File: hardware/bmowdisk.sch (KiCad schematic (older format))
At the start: 41 parts, among them CON1 IDC20, J1 MA06-1NORMAL, J2 MA04-1S, J3 LCD1, J4 M02PTH, U1 LCMXO2-1200HC-TQFP100, U2 SPI-FLASH, U3 MIC5219XX, U4 74X245, U5 74X245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

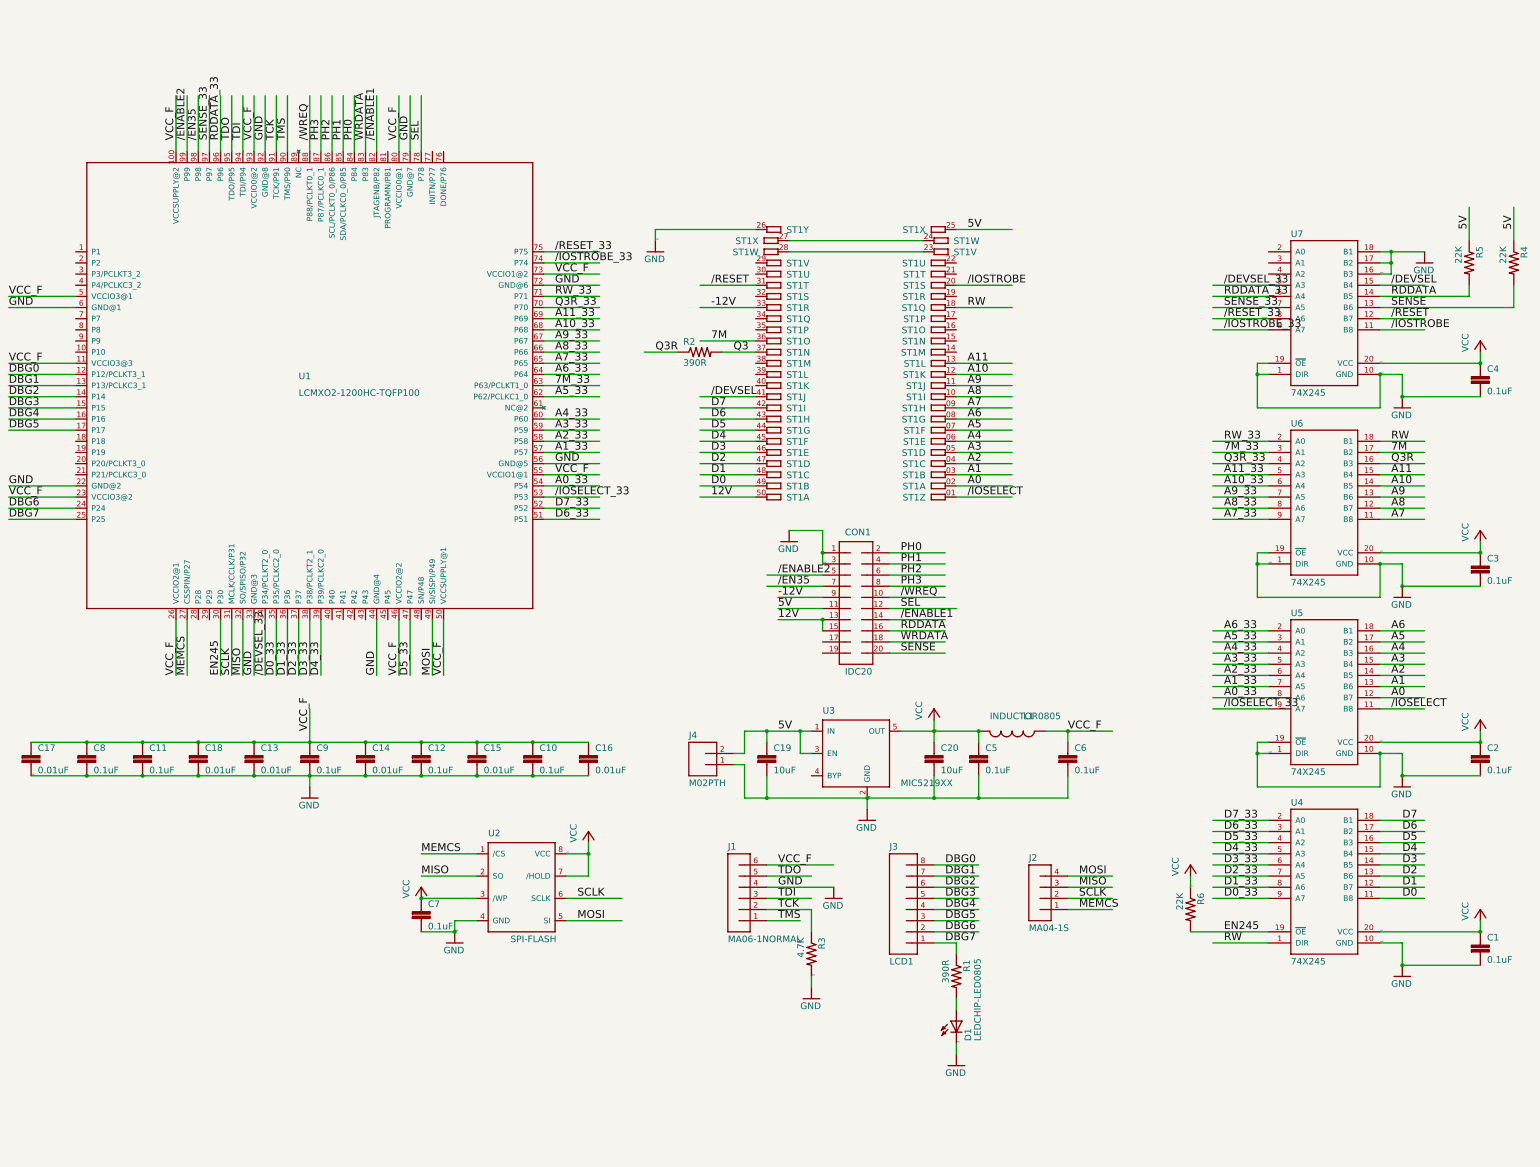
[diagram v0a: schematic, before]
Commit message: Tidy up schematics, remove machxo2 FPGA and related components
Initial prototype version with headers for connecting olimex ice40-hx8k
fpga dev board for replacing the fpga

Signed-off-by: Rangel Ivanov <rangelivanov88@gmail.com>
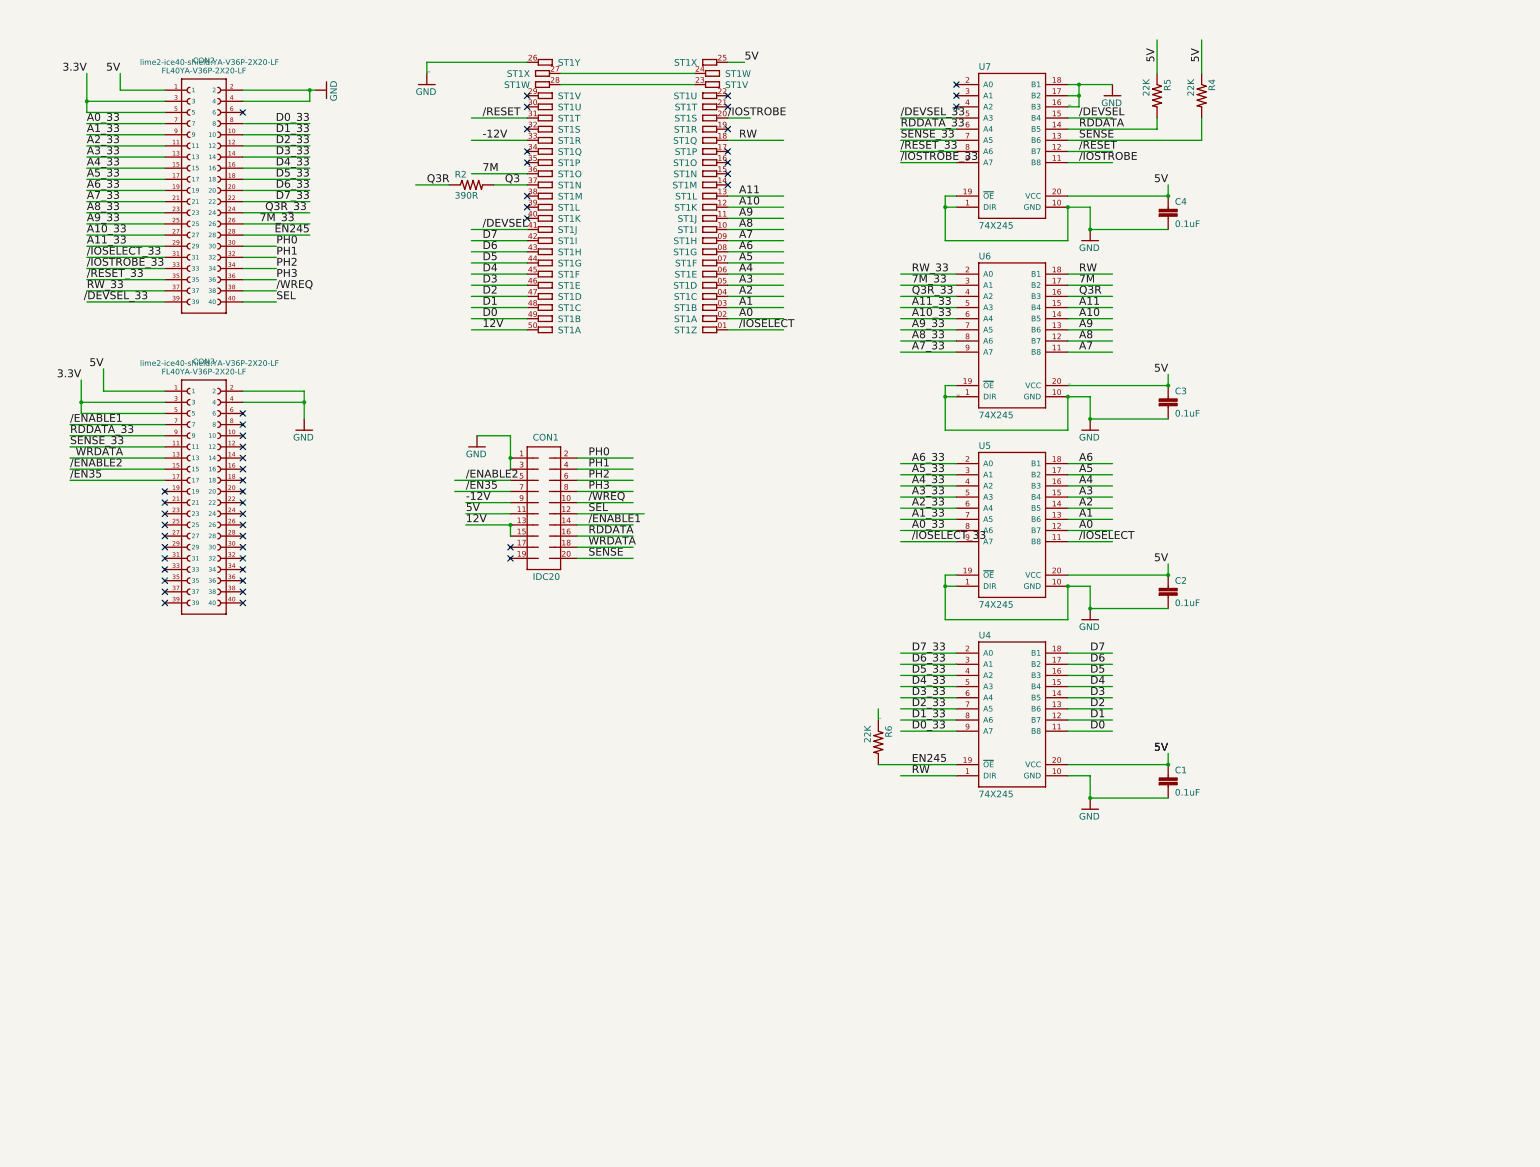
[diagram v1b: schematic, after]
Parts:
- removed C10, C11, C12, C5, C6, C7, C8, C9: 0.1uF, bmowdisk:0805, symbol bmowdisk-eagle-import:CAP0805
- removed C13, C14, C15, C16, C17, C18: 0.01uF, bmowdisk:0805, symbol bmowdisk-eagle-import:CAP0805
- removed C19, C20: 10uF, bmowdisk:0805, symbol bmowdisk-eagle-import:CAP0805
- removed D1: LEDCHIP-LED0805, bmowdisk:CHIP-LED0805, symbol bmowdisk-eagle-import:LEDCHIP-LED0805
- removed J1: MA06-1NORMAL, bmowdisk:MA06-1, symbol bmowdisk-eagle-import:MA06-1NORMAL
- removed J2: MA04-1S, bmowdisk:MA04-1, symbol bmowdisk-eagle-import:MA04-1S
- removed J3: LCD1, bmowdisk:1X08, symbol bmowdisk-eagle-import:M081X08
- removed J4: M02PTH, bmowdisk:1X02, symbol bmowdisk-eagle-import:M02PTH
- removed L1: INDUCTOR0805, bmowdisk:0805, symbol bmowdisk-eagle-import:INDUCTOR0805
- removed R1: 390R, bmowdisk:0805, symbol bmowdisk-eagle-import:RESISTOR0805-RES
- removed R3: 4.7K, bmowdisk:0805, symbol bmowdisk-eagle-import:RESISTOR0805-RES
- removed U1: LCMXO2-1200HC-TQFP100, bmowdisk:TQFP100, symbol bmowdisk-eagle-import:LCMXO2-1200HC-TQFP100
- removed U2: SPI-FLASH, bmowdisk:SOIC08, symbol bmowdisk-eagle-import:SPI-FLASH
- removed U3: MIC5219XX, bmowdisk:SOT23-5, symbol bmowdisk-eagle-import:MIC5219XX
- added CON2, CON3: FL40YA-V36P-2X20-LF, lime2-ice40-shield:YA-V36P-2X20-LF, symbol ice40-shield-lib:FL40YA-V36P-2X20-LF
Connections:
- net labels added: 3.3V
- net labels removed: DBG0, DBG1, DBG2, DBG3, DBG4, DBG5, DBG6, DBG7, MEMCS, MISO, MOSI, SCLK, TCK, TDI, TDO, TMS, VCC_F
- wire segments 323 -> 223
- no-connect marks 0 -> 50
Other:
- moved on the sheet: C1, C2, C3, C4, CON1, R2, R4, R5, R6, ST1A, ST1B, ST1C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

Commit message: Replace 74X245 with SN74LVC8T245PW
Signed-off-by: Rangel Ivanov <rangelivanov88@gmail.com>
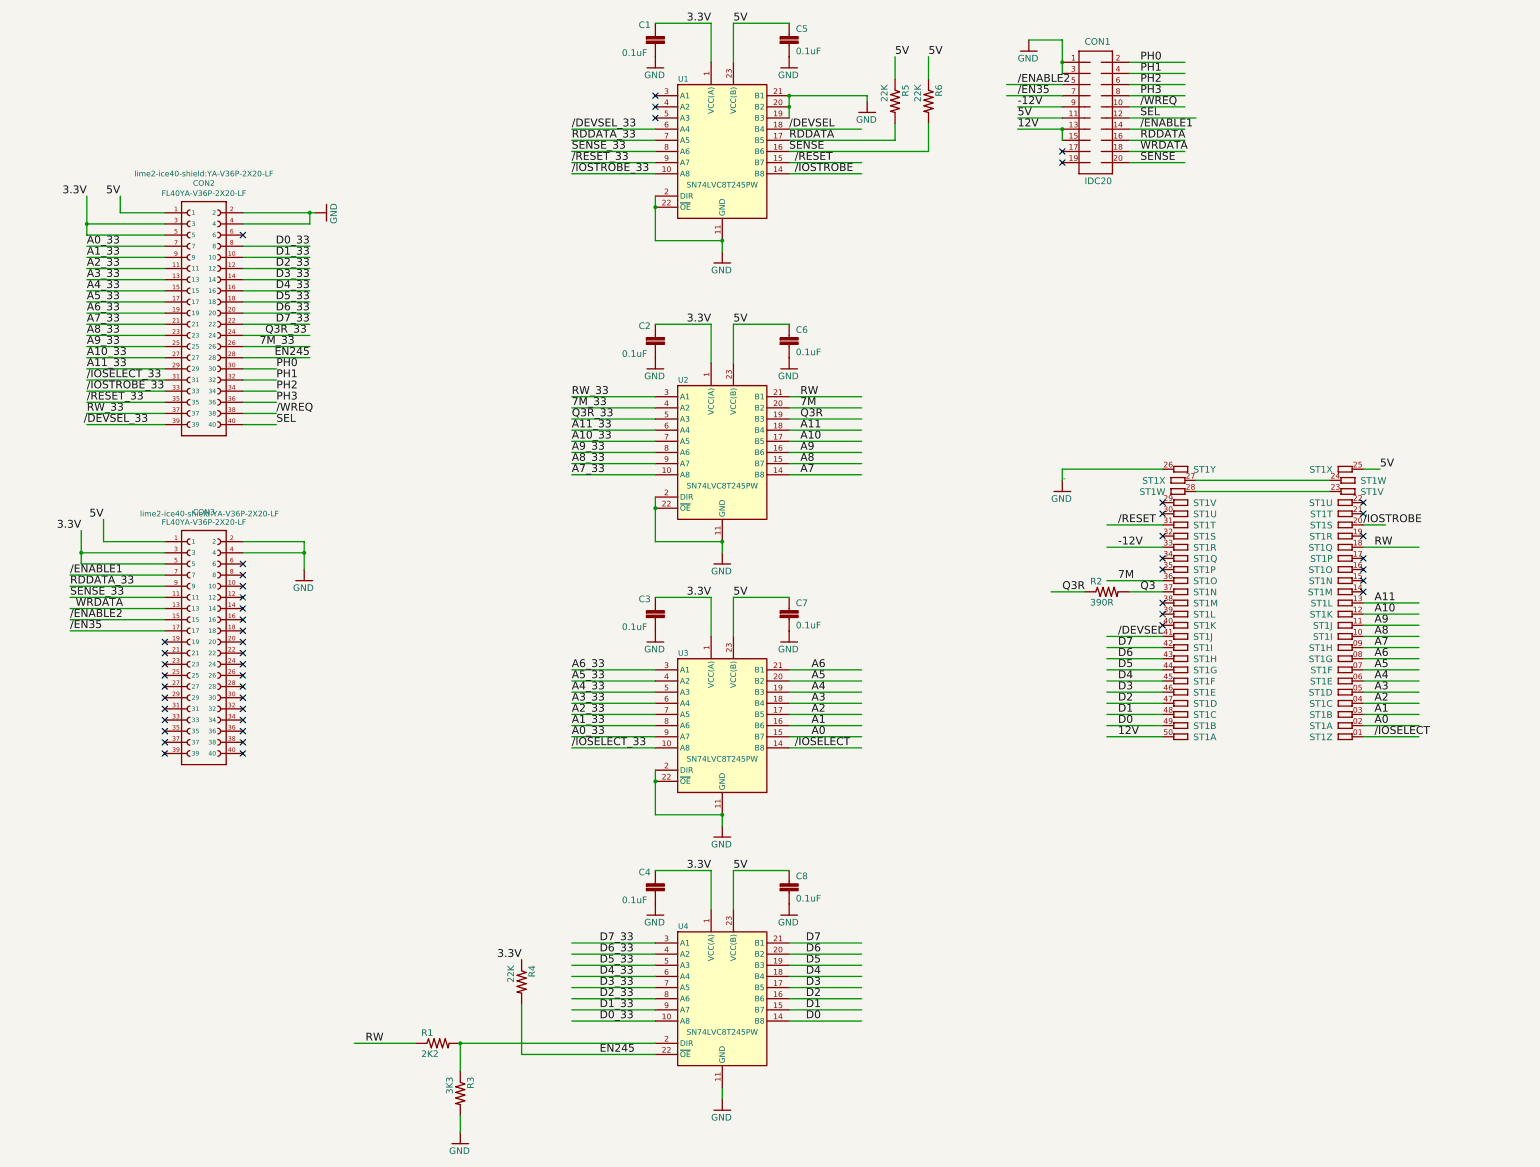
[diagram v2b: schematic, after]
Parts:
- removed U4, U5, U6, U7: 74X245, bmowdisk:SSOP20, symbol bmowdisk-eagle-import:74X245
- added C5, C6, C7, C8: 0.1uF, bmowdisk:0805, symbol bmowdisk-eagle-import:CAP0805
- added R1: 2K2, bmowdisk:0805, symbol bmowdisk-eagle-import:RESISTOR0805-RES
- added R3: 3K3, bmowdisk:0805, symbol bmowdisk-eagle-import:RESISTOR0805-RES
- added U1, U2, U3, U4: SN74LVC8T245PW, Package_SO:TSSOP-24_4.4x7.8mm_P0.65mm, symbol bmowdisk-eagle-import:SN74LVC8T245PW
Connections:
- net labels removed: VCC
- wire segments 223 -> 215
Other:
- moved on the sheet: CON1, CON2, CON3, R2, ST1A, ST1B, ST1C, ST1D, ST1E, ST1F, ST1G, ST1H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

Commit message: Lower text size of labels
Use ~ for active low labels/signals

Add TSSOP-24_4.4x7.8mm_P0.65mm footprint to project specific libs

Signed-off-by: Rangel Ivanov <rangelivanov88@gmail.com>
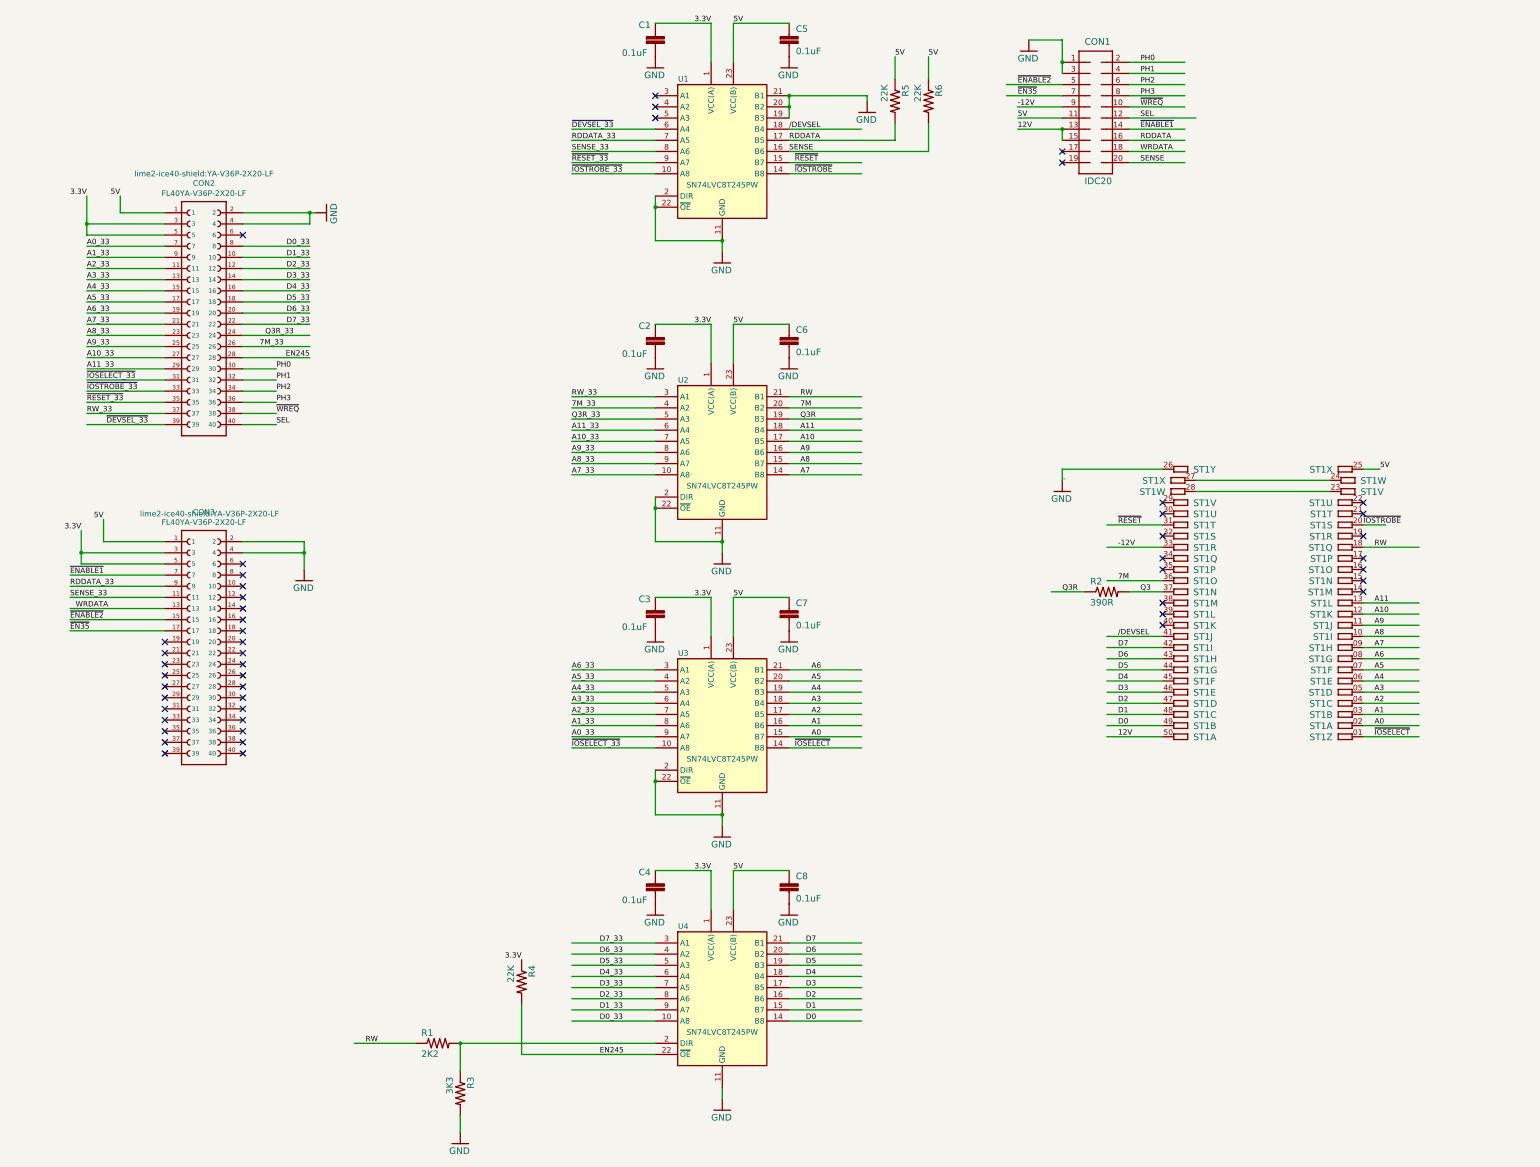
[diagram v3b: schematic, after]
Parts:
- U1, U2, U3, U4: footprint Package_SO:TSSOP-24_4.4x7.8mm_P0.65mm -> bmowdisk:TSSOP-24_4.4x7.8mm_P0.65mm
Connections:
- net labels added: ~DEVSEL_33, ~EN35, ~ENABLE1, ~ENABLE2, ~IOSELECT, ~IOSELECT_33, ~IOSTROBE, ~IOSTROBE_33, ~RESET, ~RESET_33, ~WREQ
- net labels removed: /DEVSEL_33, /EN35, /ENABLE1, /ENABLE2, /IOSELECT, /IOSELECT_33, /IOSTROBE, /IOSTROBE_33, /RESET, /RESET_33, /WREQ
